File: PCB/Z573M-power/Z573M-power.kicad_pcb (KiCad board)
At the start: 2 copper layers, 41.6 x 62.7 mm, 32 parts, among them J1 Barrel_Jack_Switch, J2 Conn_3_screw_OSTVN03A150, J3 Conn_2_screw_OSTVN02A150, Q1 IRF730 TO220-3, Q2 ZTX857, U1 LM317_TO-220

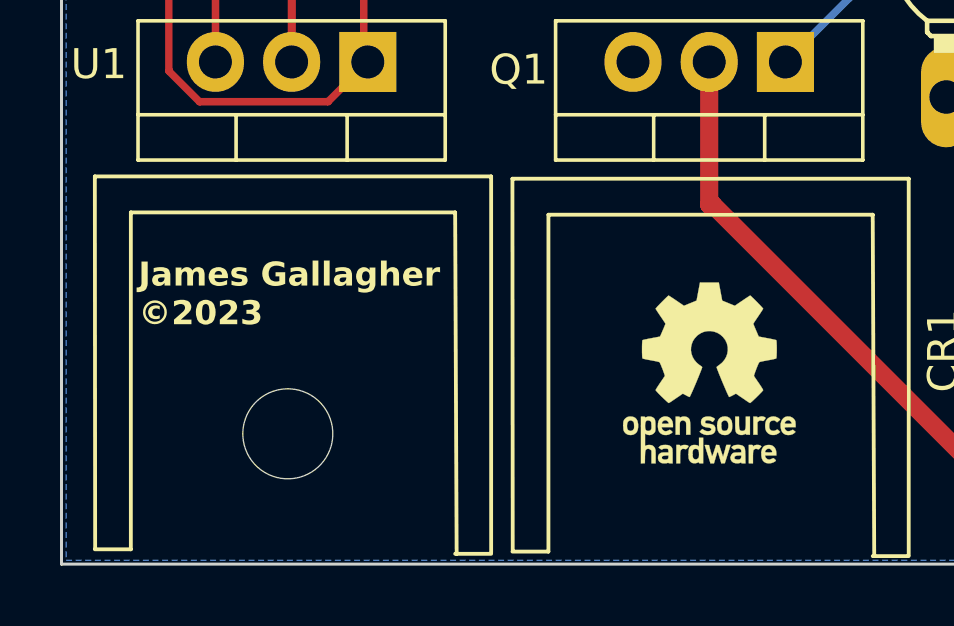
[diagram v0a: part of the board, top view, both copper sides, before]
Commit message: Added QR code to power board
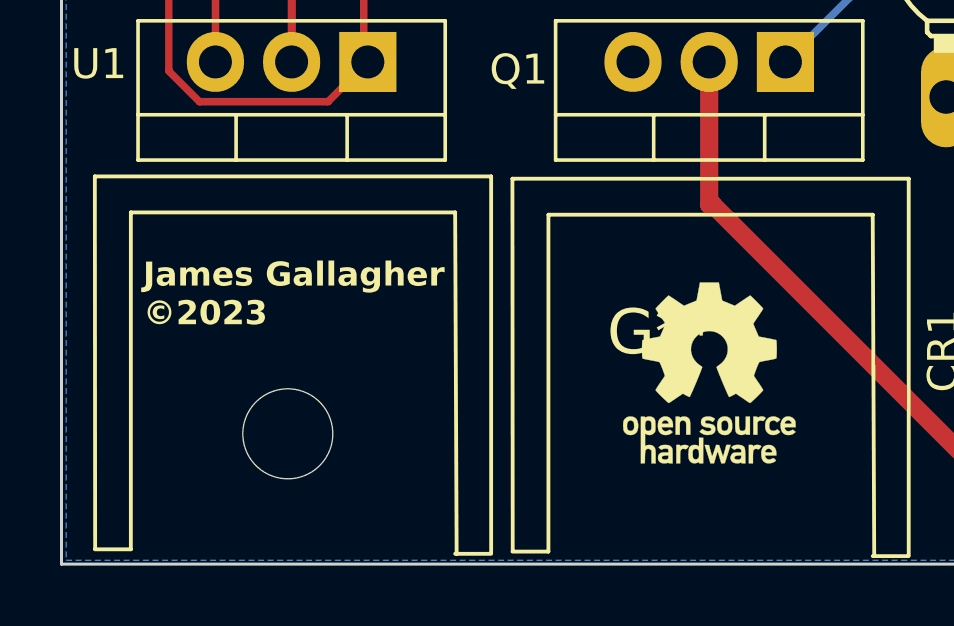
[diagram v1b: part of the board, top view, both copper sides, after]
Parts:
- added G***: LOGO, nixie-2.1-footprints:UntitledZ573M-power-pcb-14mm, B.Cu at (43.7, 78.5)

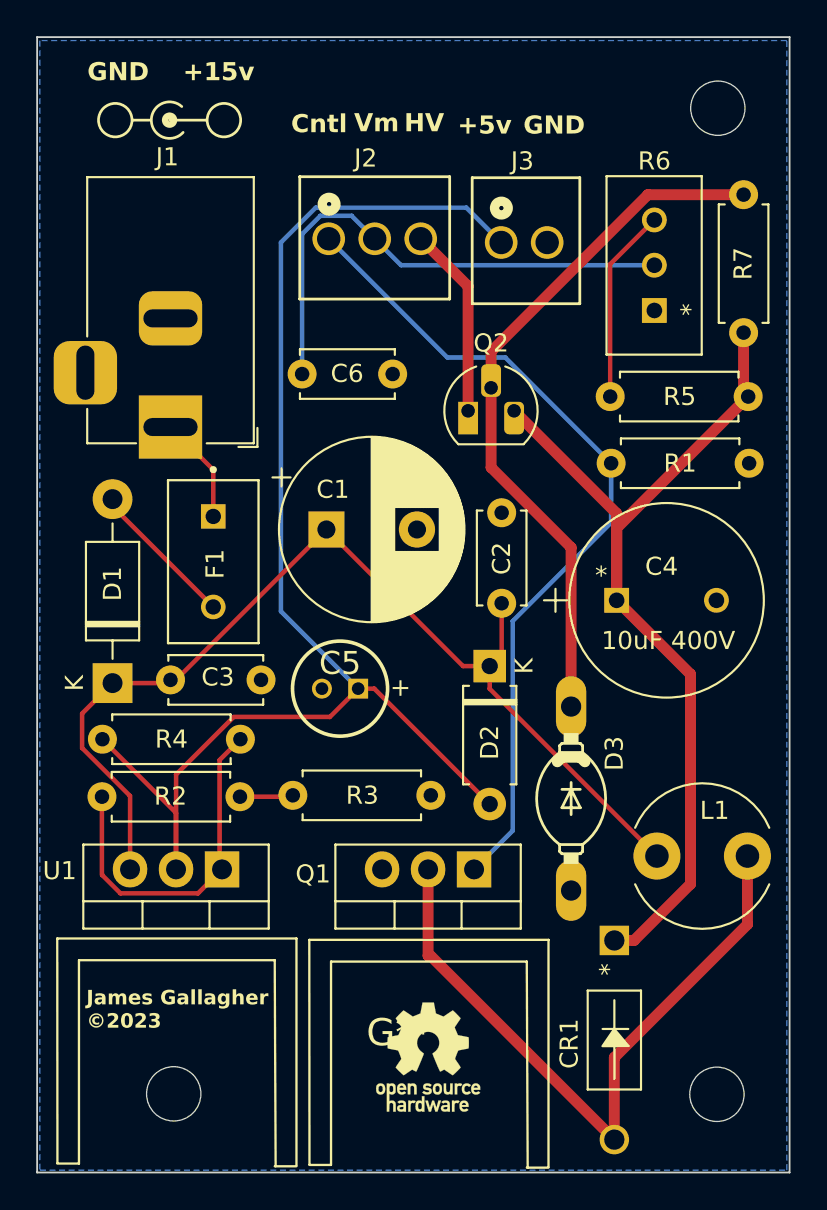
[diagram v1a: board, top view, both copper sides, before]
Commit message: Updated some traces
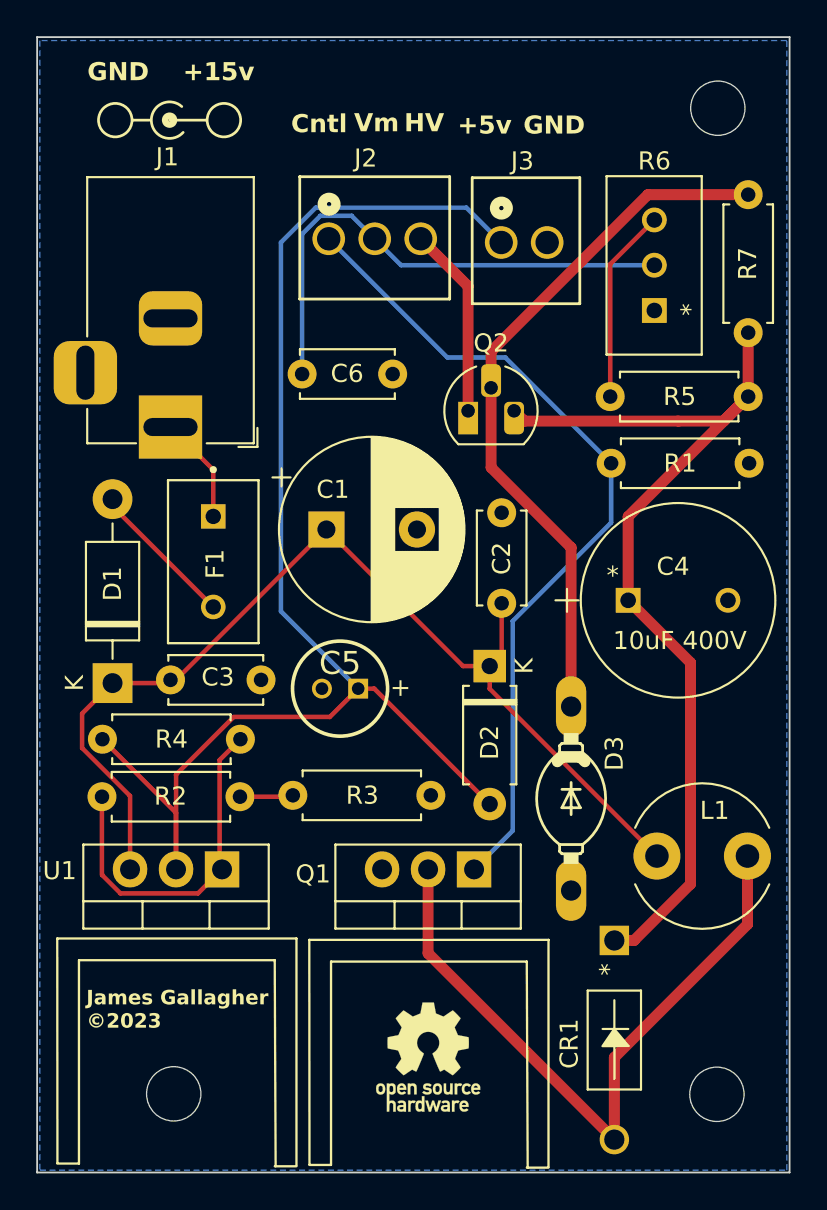
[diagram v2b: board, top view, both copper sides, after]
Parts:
- moved C4 0.63 mm to (55.8, 54.6)
- moved R7 0.25 mm to (62.5, 39.8)
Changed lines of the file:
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@@
   )
   (footprint "nixie-2.1-footprints:10uF_400v_ESG106M400AH4AA" (layer "F.Cu")
-    (at 55.1942 54.61)
+    (at 55.8292 54.61)
     (property "Sheetfile" "Z573M-power.kicad_sch")
     (property "Sheetname" "")
@@
         (effects (font (size 1 1) (thickness 0.15)))
     )
-    (fp_text value "Symbol_Barrel_Polarity" (at 0 2) (layer "F.Fab")
+    (fp_text value "Symbol_Barrel_Polarity" (at 0 2) (layer "F.Fab") hide
         (effects (font (size 1 1) (thickness 0.15)))
     )
@@
   )
   (footprint "Resistor_THT:R_Axial_DIN0207_L6.3mm_D2.5mm_P7.62mm_Horizontal" (layer "F.Cu")
-    (at 62.2046 39.8272 90)
+    (at 62.4586 39.8272 90)
     (descr "Resistor, Axial_DIN0207 series, Axial, Horizontal, pin pitch=7.62mm, 0.25W = 1/4W, length*diameter=6.3*2.5mm^2, http://cdn-reichelt.de/documents/datenblatt/B400/1_4W%23YAG.pdf")
     (tags "Resistor Axial_DIN0207 series Axial Horizontal pin pitch 7.62mm 0.25W = 1/4W length 6.3mm diameter 2.5mm")
@@
     (at 43.7134 78.486 180)
     (attr board_only exclude_from_pos_files exclude_from_bom)
-    (fp_text reference "G***" (at 0 0) (layer "F.SilkS")
+    (fp_text reference "G***" (at 0 0) (layer "F.SilkS") hide
         (effects (font (size 1.5 1.5) (thickness 0.3)))
     )
@@
   (segment (start 48.1838 59.4976) (end 57.4186 68.7324) (width 0.25) (layer "F.Cu") (net 1))
   (segment (start 48.1838 58.2422) (end 48.1838 59.4976) (width 0.25) (layer "F.Cu") (net 1))
-  (segment (start 55.1942 49.8094) (end 55.1942 54.61) (width 0.606715) (layer "F.Cu") (net 3))
-  (segment (start 62.2046 43.1038) (end 62.4586 43.3578) (width 0.606715) (layer "F.Cu") (net 3))
-  (segment (start 59.271957 58.687757) (end 55.1942 54.61) (width 0.606715) (layer "F.Cu") (net 3))
-  (segment (start 56.1594 73.3935) (end 59.271957 70.280943) (width 0.606715) (layer "F.Cu") (net 3))
-  (segment (start 49.53 44.1452) (end 55.1942 49.8094) (width 0.606715) (layer "F.Cu") (net 3))
-  (segment (start 62.4586 43.3578) (end 55.1942 50.6222) (width 0.606715) (layer "F.Cu") (net 3))
-  (segment (start 55.1942 50.6222) (end 55.1942 54.61) (width 0.606715) (layer "F.Cu") (net 3))
-  (segment (start 59.271957 70.280943) (end 59.271957 58.687757) (width 0.606715) (layer "F.Cu") (net 3))
-  (segment (start 55.0672 73.3935) (end 56.1594 73.3935) (width 0.606715) (layer "F.Cu") (net 3))
-  (segment (start 62.2046 39.8272) (end 62.2046 43.1038) (width 0.606715) (layer "F.Cu") (net 3))
+  (segment (start 62.4586 39.8272) (end 62.4586 43.3578) (width 0.606715) (layer "F.Cu") (net 3))
+  (segment (start 49.53 44.1452) (end 50.095957 44.711157) (width 0.606715) (layer "F.Cu") (net 3))
+  (segment (start 50.095957 44.711157) (end 58.5978 44.711157) (width 0.606715) (layer "F.Cu") (net 3))
+  (segment (start 61.105243 44.711157) (end 62.4586 43.3578) (width 0.606715) (layer "F.Cu") (net 3))
+  (segment (start 56.1594 73.3935) (end 55.0672 73.3935) (width 0.606715) (layer "F.Cu") (net 3))
+  (segment (start 58.5978 44.711157) (end 61.105243 44.711157) (width 0.606715) (layer "F.Cu") (net 3))
+  (segment (start 59.271957 70.280943) (end 56.1594 73.3935) (width 0.606715) (layer "F.Cu") (net 3))
+  (segment (start 55.8292 49.9872) (end 62.4586 43.3578) (width 0.606715) (layer "F.Cu") (net 3))
+  (segment (start 55.8292 54.61) (end 55.8292 49.9872) (width 0.606715) (layer "F.Cu") (net 3))
+  (segment (start 55.8292 54.61) (end 59.271957 58.052757) (width 0.606715) (layer "F.Cu") (net 3))
+  (segment (start 59.271957 58.052757) (end 59.271957 70.280943) (width 0.606715) (layer "F.Cu") (net 3))
   (segment (start 41.8084 59.4868) (end 48.1838 65.8622) (width 0.25) (layer "F.Cu") (net 4))
   (segment (start 30.861 66.3448) (end 30.861 69.469) (width 0.25) (layer "F.Cu") (net 4))
@@
   (segment (start 40.565799 33.3756) (end 41.8338 34.643601) (width 0.25) (layer "B.Cu") (net 5))
   (segment (start 38.826985 33.3756) (end 40.565799 33.3756) (width 0.25) (layer "B.Cu") (net 5))
-  (segment (start 44.7802 69.469) (end 44.7802 74.2317) (width 0.606715) (layer "F.Cu") (net 6))
-  (segment (start 44.9072 74.2317) (end 44.7802 74.2317) (width 0.606715) (layer "F.Cu") (net 6))
   (segment (start 55.0672 79.8576) (end 62.4186 72.5062) (width 0.606715) (layer "F.Cu") (net 6))
-  (segment (start 55.0672 84.3917) (end 44.9072 74.2317) (width 0.606715) (layer "F.Cu") (net 6))
+  (segment (start 44.7802 69.469) (end 44.7802 74.1047) (width 0.606715) (layer "F.Cu") (net 6))
   (segment (start 55.0672 84.3917) (end 55.0672 79.8576) (width 0.606715) (layer "F.Cu") (net 6))
+  (segment (start 44.7802 74.1047) (end 55.0672 84.3917) (width 0.606715) (layer "F.Cu") (net 6))
   (segment (start 62.4186 72.5062) (end 62.4186 68.7324) (width 0.606715) (layer "F.Cu") (net 6))
   (segment (start 32.9184 54.9764) (end 27.3558 49.4138) (width 0.25) (layer "F.Cu") (net 7))
@@
   (segment (start 46.99 37.259801) (end 44.3738 34.643601) (width 0.606715) (layer "F.Cu") (net 10))
   (segment (start 46.99 44.1452) (end 46.99 37.259801) (width 0.606715) (layer "F.Cu") (net 10))
-  (segment (start 62.2046 32.2072) (end 56.921567 32.2072) (width 0.606715) (layer "F.Cu") (net 11))
-  (segment (start 56.921567 32.2072) (end 48.26 40.868767) (width 0.606715) (layer "F.Cu") (net 11))
-  (segment (start 48.26 40.868767) (end 48.26 42.8752) (width 0.606715) (layer "F.Cu") (net 11))
   (segment (start 52.6796 60.4774) (end 52.6796 51.694664) (width 0.606715) (layer "F.Cu") (net 11))
+  (segment (start 56.921567 32.2072) (end 48.26 40.868767) (width 0.606715) (layer "F.Cu") (net 11))
+  (segment (start 62.4586 32.2072) (end 56.921567 32.2072) (width 0.606715) (layer "F.Cu") (net 11))
   (segment (start 48.26 47.275064) (end 48.26 42.8752) (width 0.606715) (layer "F.Cu") (net 11))
   (segment (start 52.6796 51.694664) (end 48.26 47.275064) (width 0.606715) (layer "F.Cu") (net 11))
+  (segment (start 48.26 40.868767) (end 48.26 42.8752) (width 0.606715) (layer "F.Cu") (net 11))
   (segment (start 33.401 69.469) (end 33.2666 69.3346) (width 0.25) (layer "F.Cu") (net 12))
   (segment (start 33.2666 69.3346) (end 33.2666 63.4312) (width 0.25) (layer "F.Cu") (net 12))
